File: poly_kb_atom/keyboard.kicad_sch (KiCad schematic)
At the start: 8 parts, among them J2 North, J3 WestFront, J4 EastFront, J5 WestBack, J6 EastBack, J7 South, J8 North2, J9 South2

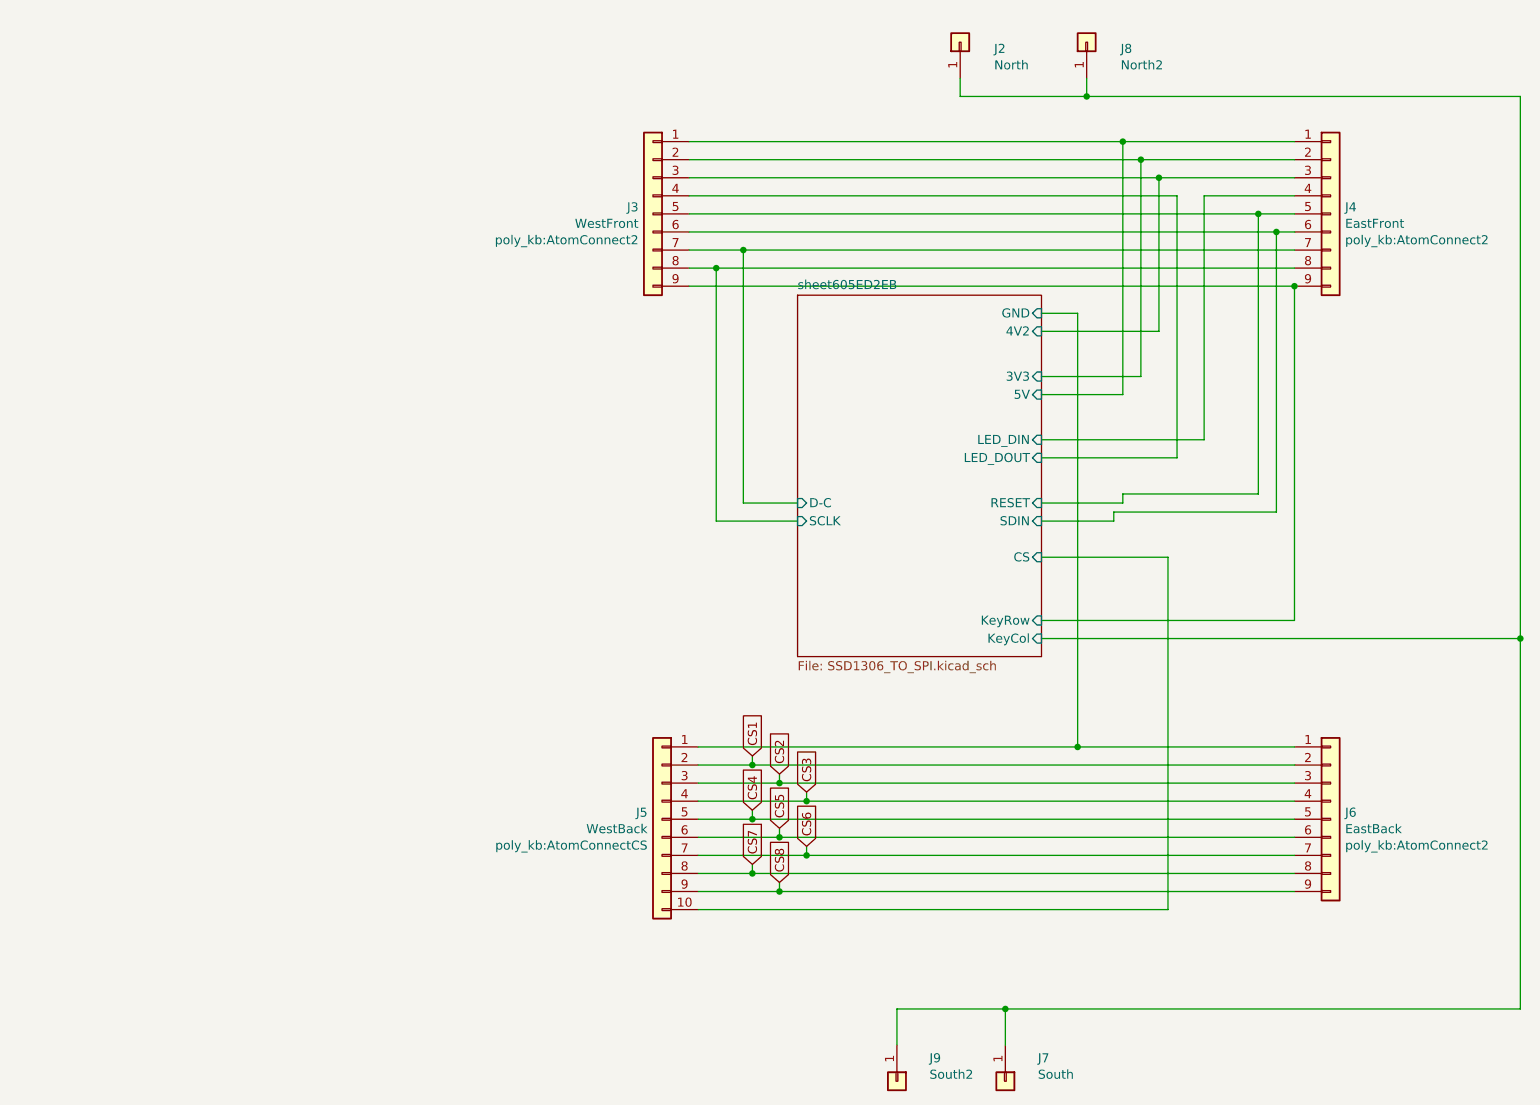
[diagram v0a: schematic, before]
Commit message: Added new revisions for all pcbs expect 1.25U; cleaned up gerber dirs
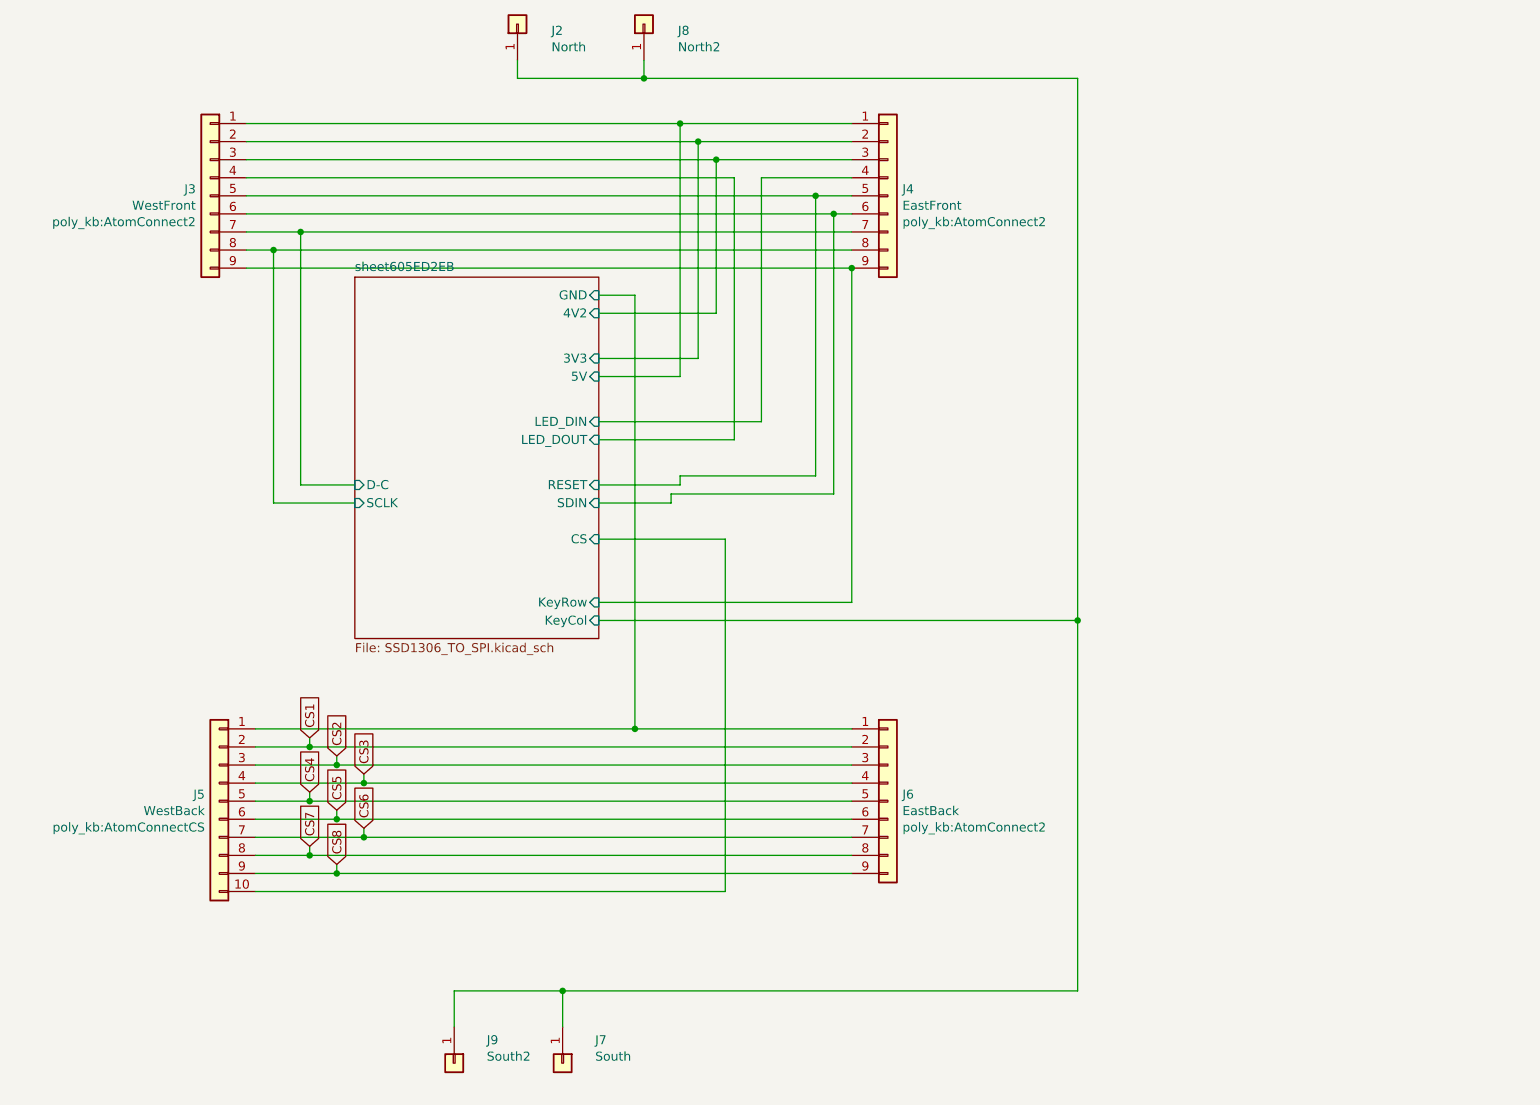
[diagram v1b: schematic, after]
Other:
- moved on the sheet: J2, J3, J4, J5, J6, J7, J8, J9
